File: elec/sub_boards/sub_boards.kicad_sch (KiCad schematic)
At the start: 29 parts, among them J1 Raspberry_Pi_5, J3 2.54mm PinHeader, J4 2.54mm PinHeader, J5 EncSide, J6 EncSide, J7 B2B-XH, Q1 ST-1KL3A, Q2 ST-1KL3A, Q3 ST-1KL3A, Q4 ST-1KL3A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

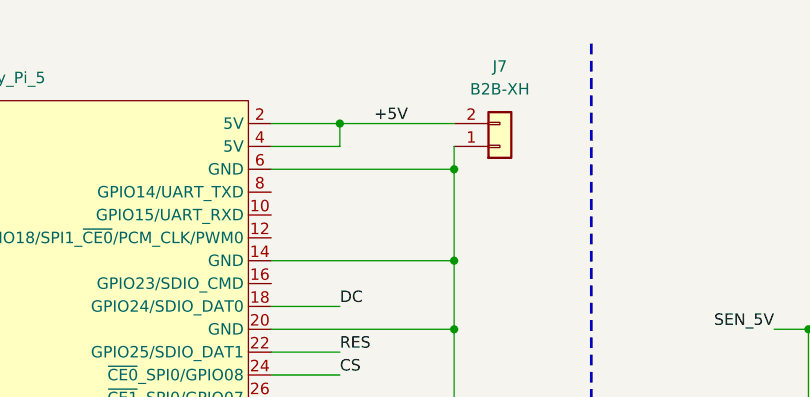
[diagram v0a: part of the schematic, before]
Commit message: サブボード（IFボード）を修正
Signed-off-by: Kazuki Iida <elkel53930@gmail.com>
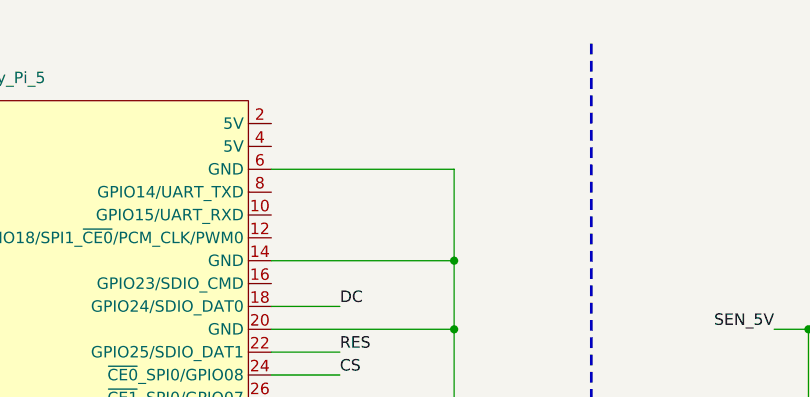
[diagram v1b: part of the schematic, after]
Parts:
- removed J7: B2B-XH, Connector_JST:JST_XH_B2B-XH-AM_1x02_P2.50mm_Vertical, symbol Connector_Generic:Conn_01x02
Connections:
- net +5V: no longer names the net of J1.2 (5V)
- net +5V: no longer J1.4 (5V)
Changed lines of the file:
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@@
-	)
-	(junction
-		(at 121.92 36.83)
-		(diameter 0)
-		(color 0 0 0 0)
 	)
 	(junction
@@
 	)
 	(junction
-		(at 109.22 31.75)
-		(diameter 0)
-		(color 0 0 0 0)
-	)
-	(junction
 		(at 161.29 72.39)
 		(diameter 0)
@@
 	(wire
 		(pts
-			(xy 101.6 34.29) (xy 109.22 34.29)
-		)
-		(stroke
-			(width 0)
-			(type default)
-		)
-	)
-	(wire
-		(pts
 			(xy 156.21 111.76) (xy 156.21 134.62)
 		)
@@
 	(wire
 		(pts
-			(xy 101.6 31.75) (xy 109.22 31.75)
-		)
-		(stroke
-			(width 0)
-			(type default)
-		)
-	)
-	(wire
-		(pts
 			(xy 77.47 119.38) (xy 77.47 127)
 		)
@@
 		(pts
 			(xy 38.1 41.91) (xy 19.05 41.91)
-		)
-		(stroke
-			(width 0)
-			(type default)
-		)
-	)
-	(wire
-		(pts
-			(xy 109.22 31.75) (xy 109.22 34.29)
 		)
 		(stroke
@@
 	(wire
 		(pts
-			(xy 121.92 31.75) (xy 109.22 31.75)
-		)
-		(stroke
-			(width 0)
-			(type default)
-		)
-	)
-	(wire
-		(pts
 			(xy 160.02 109.22) (xy 160.02 127)
 		)
@@
 		(pts
 			(xy 74.93 156.21) (xy 78.74 156.21)
-		)
-		(stroke
-			(width 0)
-			(type default)
-		)
-	)
-	(wire
-		(pts
-			(xy 121.92 34.29) (xy 121.92 36.83)
 		)
 		(stroke
@@
 			)
 			(justify right bottom)
-		)
-	)
-	(label "+5V"
-		(at 113.03 31.75 0)
-		(effects
-			(font
-				(size 1.27 1.27)
-			)
-			(justify left bottom)
 		)
 	)
@@
 					(unit 1)
 				)
-			)
-		)
-	)
-	(symbol
-		(lib_id "Connector_Generic:Conn_01x02")
-		(at 127 34.29 0)
-		(mirror x)
-		(unit 1)
-		(exclude_from_sim no)
-		(in_bom yes)
-		(on_board yes)
-		(dnp no)
-		(property "Reference" "J7"
-			(at 127 25.4 0)
-			(effects
-				(font
-					(size 1.27 1.27)
-				)
-			)
-		)
-		(property "Value" "B2B-XH"
-			(at 127 27.94 0)
-			(effects
-				(font
-					(size 1.27 1.27)
-				)
-			)
-		)
-		(property "Footprint" "Connector_JST:JST_XH_B2B-XH-AM_1x02_P2.50mm_Vertical"
-			(at 127 34.29 0)
-			(effects
-				(font
-					(size 1.27 1.27)
-				)
-				(hide yes)
-			)
-		)
-		(property "Datasheet" "~"
-			(at 127 34.29 0)
-			(effects
-				(font
-					(size 1.27 1.27)
-				)
-				(hide yes)
-			)
-		)
-		(property "Description" "Generic connector, single row, 01x02, script generated (kicad-library-utils/schlib/autogen/connector/)"
-			(at 127 34.29 0)
-			(effects
-				(font
-					(size 1.27 1.27)
-				)
-				(hide yes)
-			)
-		)
-		(pin "2"
-		)
-		(pin "1"
-		)
-		(instances
-			(project ""
-				(path "/6d352afe-5946-44c0-9310-c43eb184c15e"
-					(reference "J7")
-					(unit 1)
-				)
